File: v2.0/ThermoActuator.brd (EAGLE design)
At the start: 99.1 x 80 mm, 72 parts, among them IC1 ULN2003AD, IC2 PCF8574T, U1 CD74HCT4051_D_16

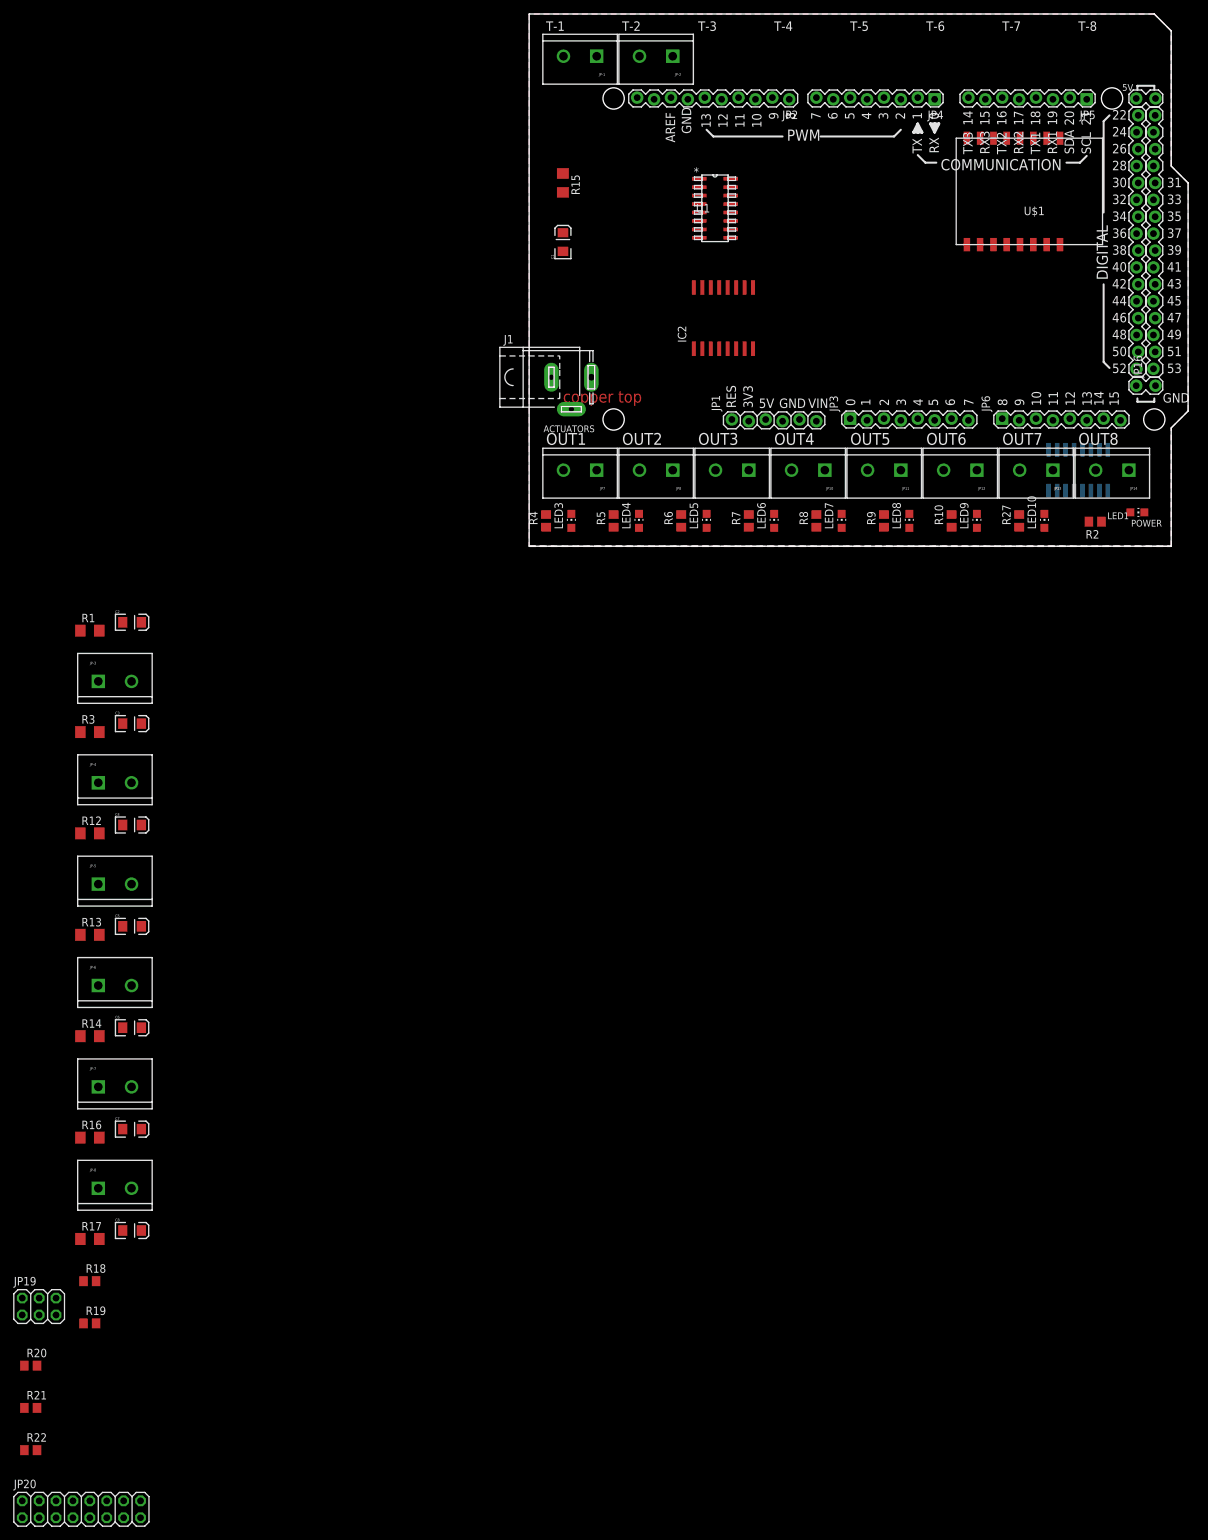
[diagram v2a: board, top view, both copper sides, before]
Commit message: PCB caped for lower profile
two capes are cut. All components are thrown on the PCB
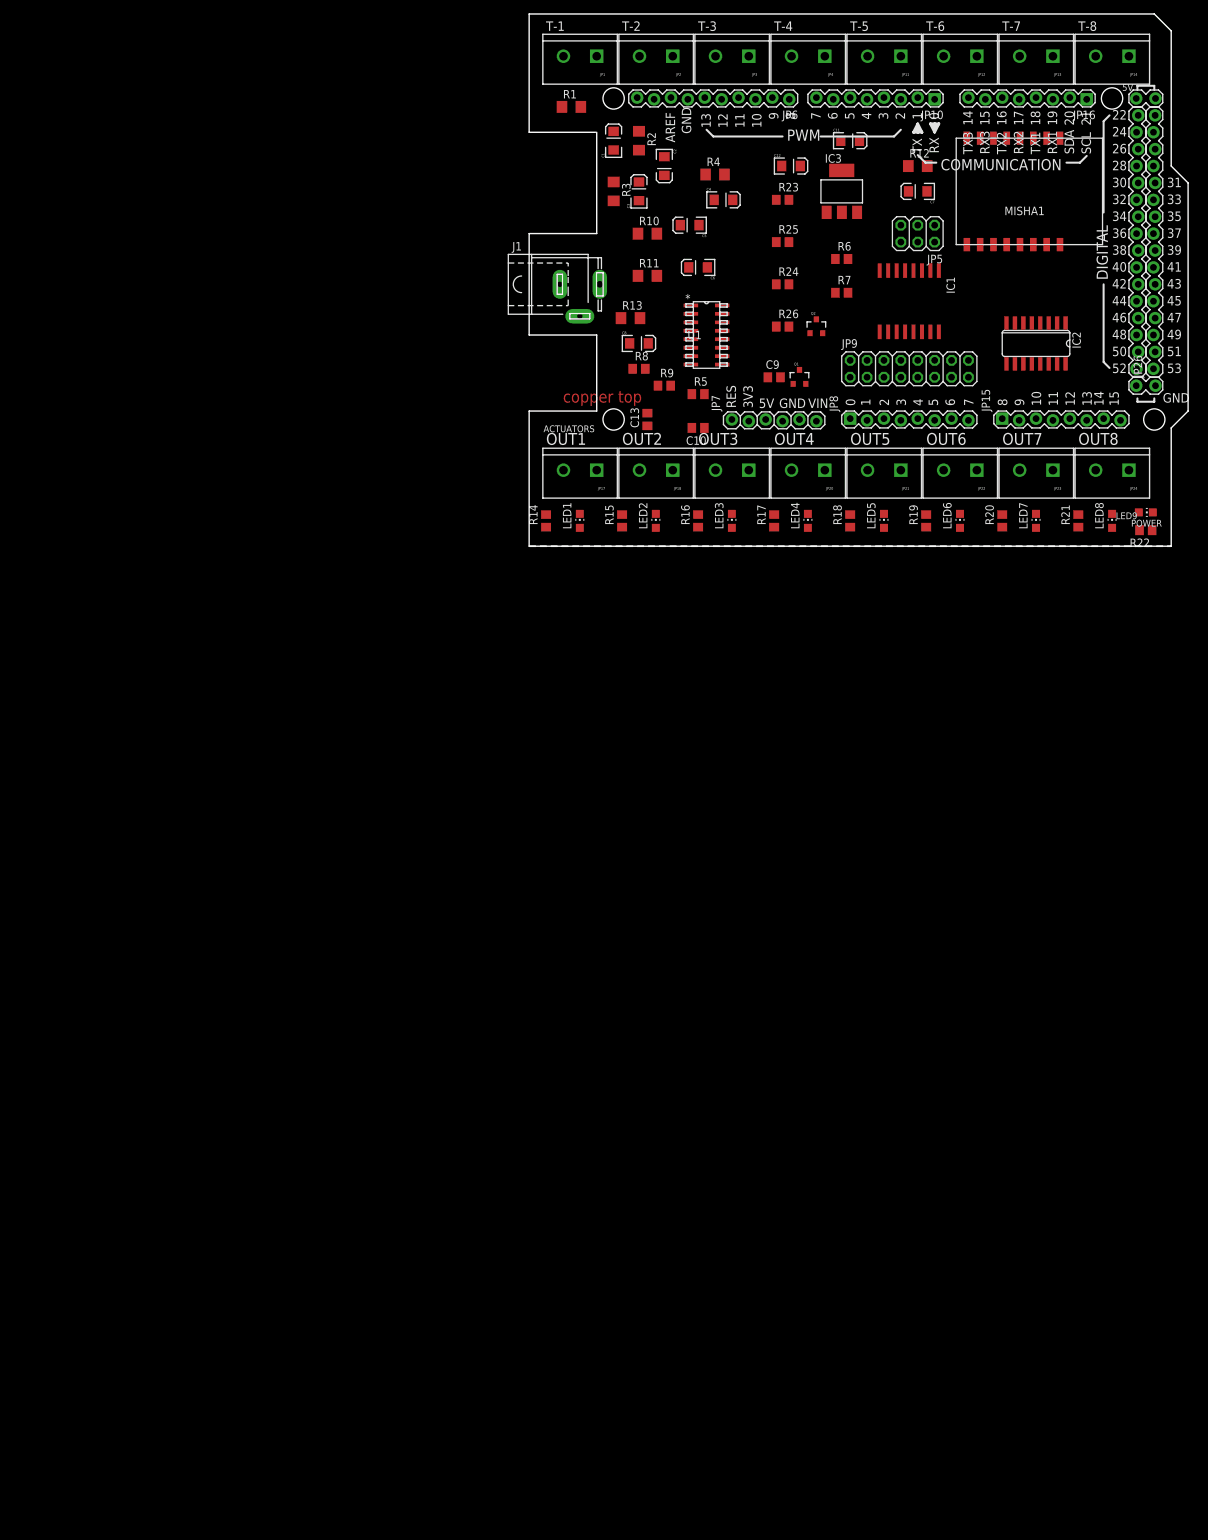
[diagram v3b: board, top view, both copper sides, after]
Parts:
- removed JP-1, JP-2, JP-3, JP-4, JP-5, JP-6, JP-7, JP-8: M025MM, SparkFun-Connectors:SCREWTERMINAL-5MM-2
- removed LED10: Blue, led:CHIP-LED0805
- removed R27: 330, rcl:R0805
- added C10, C13, C9: 100nF, rcl:C0805
- added C11, C12: 5uF, SparkFun-Capacitors:EIA3216
- added IC3: REG1117, burr-brown:SOT223
- added JP21, JP22, JP23, JP24: M025MM, SparkFun-Connectors:SCREWTERMINAL-5MM-2
- added JP25, JP28: (no value), SparkFun:1X02_LOCK
- added JP26, JP27: M16LOCK, SparkFun:1X16_LOCK
- added LED2: White, led:CHIP-LED0805
- added Q1, Q2: 200mA/50V, SparkFun-DiscreteSemi:SOT23-3
- added R11: 1K, rcl:R1206
- added R23, R24, R25, R26: 10K, rcl:R0805
- IC1: value ULN2003AD -> PCF8574T; device uln-udn:SO16 -> micro-philips:SO16W
- IC2: value PCF8574T -> ULN2003AD; device micro-philips:SO16W -> uln-udn:SO16
- JP1: value (none) -> M025MM; device SparkFun:1X06_LOCK -> SparkFun-Connectors:SCREWTERMINAL-5MM-2
- JP10, JP8: value M025MM -> (none); device SparkFun-Connectors:SCREWTERMINAL-5MM-2 -> SparkFun:1X08_LOCK
- JP15: device SparkFun:1X02_LOCK -> SparkFun:1X08_LOCK
- JP16: value M16LOCK -> (none); device SparkFun:1X16_LOCK -> SparkFun:1X08_LOCK
- JP17: value M16LOCK -> M025MM; device SparkFun:1X16_LOCK -> SparkFun-Connectors:SCREWTERMINAL-5MM-2
- JP18: value (none) -> M025MM; device SparkFun:1X02_LOCK -> SparkFun-Connectors:SCREWTERMINAL-5MM-2
- JP19: value (none) -> M025MM; device pinhead:2X03 -> SparkFun-Connectors:SCREWTERMINAL-5MM-2
- JP2: value M10LOCK -> M025MM; device SparkFun-Connectors:1X10_LOCK -> SparkFun-Connectors:SCREWTERMINAL-5MM-2
- JP20: value (none) -> M025MM; device pinhead:2X08 -> SparkFun-Connectors:SCREWTERMINAL-5MM-2
- JP3, JP4: value (none) -> M025MM; device SparkFun:1X08_LOCK -> SparkFun-Connectors:SCREWTERMINAL-5MM-2
- JP5: device SparkFun:1X08_LOCK -> pinhead:2X03
- JP6: value (none) -> M10LOCK; device SparkFun:1X08_LOCK -> SparkFun-Connectors:1X10_LOCK
- JP7: value M025MM -> (none); device SparkFun-Connectors:SCREWTERMINAL-5MM-2 -> SparkFun:1X06_LOCK
- JP9: value M025MM -> (none); device SparkFun-Connectors:SCREWTERMINAL-5MM-2 -> pinhead:2X08
- LED1: value Red -> White
- LED3, LED4, LED5, LED6, LED7, LED8: value Blue -> White
- R10, R2, R4: value 330 -> 1K; device rcl:R0805 -> rcl:R1206
- R14, R15, R16, R17: value 1K -> 3K3; device rcl:R1206 -> rcl:R0805
- R18, R19: value 330 -> 3K3
- R20, R21, R22: value 1K -> 3K3
- R5, R6, R7: value 330 -> 1K
- R8, R9: value 330 -> 4K7
- moved R22 217.3 mm to (92.7, 2.41), turned to 180 degrees
- moved R21 206.4 mm to (82.5, 3.81), turned to 90 degrees
- moved R20 193.5 mm to (71.1, 3.81), turned to 90 degrees
- moved JP20 192.1 mm to (44.5, 11.4), turned to 180 degrees
- moved C7 183.9 mm to (58.4, 53.3), turned to 180 degrees
- moved R19 174.3 mm to (59.7, 3.81), turned to 90 degrees
- moved JP19 164.9 mm to (33.0, 11.4), turned to 180 degrees
- moved R18 161.6 mm to (48.3, 3.81), turned to 90 degrees
- moved R12 159.9 mm to (58.4, 57.1)
- moved C8 153.6 mm to (16.5, 30.5)
- moved R17 149.1 mm to (36.8, 3.81), turned to 90 degrees
- moved C6 142.5 mm to (25.4, 41.9), turned to 180 degrees
- moved C5 134.7 mm to (24.1, 48.3), turned to 180 degrees
- moved R16 130.2 mm to (25.4, 3.81), turned to 90 degrees
- moved C4 129.4 mm to (29.2, 52.1)
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- renumbered U$1 to MISHA1
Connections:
- removed net D16: JP5.6
- removed net D17: JP5.5
- removed net D18: JP5.4
- removed net D19: JP5.3
- removed net GND: C1.C, C2.C, C3.C, C4.C, C5.C, C6.C, C7.C, C8.C, IC1.8, IC2.8, JP-1.1, JP-2.1, JP-3.1, JP-4.1, JP-5.1, JP-6.1, JP-7.1, JP-8.1, JP1.4, JP1.5, JP14.1, JP18.1, JP18.2, JP19.1, JP19.3, JP19.5, JP2.7, LED1.C, MISHA1.GND, U1.6, U1.7, U1.8
- removed net VCC: MISHA1.VCC
- new net 3V3: C12.A, C13.1, IC3.2, MISHA1.CH_PD, MISHA1.REST, MISHA1.VCC, Q1.1, Q2.1, R23.2, R24.2
- new net N$40: MISHA1.TXD, Q1.2, R23.1
- new net N$41: MISHA1.RXD, Q2.2, R24.1
- new net NNN: C1.C, C10.2, C11.C, C12.C, C13.2, C2.C, C3.C, C4.C, C5.C, C6.C, C7.C, C8.C, C9.2, IC1.8, IC2.8, IC3.1, J1.1, JP1.1, JP11.1, JP12.1, JP13.1, JP14.1, JP2.1, JP24.1, JP28.1, JP28.2, JP3.1, JP4.1, JP5.1, JP5.3, JP5.5, JP6.7, JP7.4, JP7.5, LED9.C, MISHA1.GND, U1.6, U1.7, U1.8
- new net RX1: JP16.3
- new net RX2: JP16.5, Q1.3, R25.1
- new net TX0: JP10.2
- new net TX2: JP16.6, Q2.3, R26.1
- net 3.3: now also JP7.2; no longer JP1.2
- net 5V: now also JP7.3; no longer JP1.3
- net AO0: now also IC2.16, JP17.2, LED1.C; no longer IC1.16, JP7.2, LED3.C
- net AO1: now also IC2.15, JP18.2, LED2.C; no longer IC1.15, JP8.2, LED4.C
- net AO2: now also IC2.14, JP19.2, LED3.C; no longer IC1.14, JP9.2, LED5.C
- net AO3: now also IC2.13, JP20.2, LED4.C; no longer IC1.13, JP10.2, LED6.C
- net AO4: now also IC2.12, JP21.2, LED5.C; no longer IC1.12, JP11.2, LED7.C
- net AO5: now also IC2.11, JP22.2, LED6.C; no longer IC1.11, JP12.2, LED8.C
- net AO6: now also IC2.10, JP23.2, LED7.C; no longer IC1.10, JP13.2, LED9.C
- net AO7: now also IC1.12, JP24.2, LED8.C; no longer JP14.2, LED10.C
- net AREF: now also JP6.8; no longer JP2.8
- net AS0: now also R1.2; no longer R15.2
- net AS1: now also R2.2; no longer R1.2
- net AS3: now also R4.2; no longer R12.2
- net AS4: now also R10.2; no longer R13.2
- net AS5: now also R11.2; no longer R14.2
- net AS6: now also R12.2; no longer R16.2
- net AS7: now also R13.2; no longer R17.2
- net D10: now also JP6.3, U1.9; no longer JP2.3
- net D11: now also JP6.4; no longer JP2.4
- net D12: now also JP6.5; no longer JP2.5
- net D13: now also JP6.6; no longer JP2.6
- net D14: now also JP16.8; no longer JP5.8
- net D15: now also JP16.7; no longer JP5.7
- net D2: now also JP10.3; no longer JP4.3
- net D22: now also JP27.1; no longer JP17.1
- net D23: now also JP26.16; no longer JP16.16
- net D24: now also JP27.2; no longer JP17.2
- net D25: now also JP26.15; no longer JP16.15
- net D26: now also JP27.3; no longer JP17.3
- net D27: now also JP26.14; no longer JP16.14
- net D28: now also JP27.4; no longer JP17.4
- net D29: now also JP26.13; no longer JP16.13
- net D3: now also JP10.4; no longer JP4.4
- net D30: now also JP27.5; no longer JP17.5
- net D31: now also JP26.12; no longer JP16.12
- net D32: now also JP27.6; no longer JP17.6
- net D33: now also JP26.11; no longer JP16.11
- net D34: now also JP27.7; no longer JP17.7
- net D35: now also JP26.10; no longer JP16.10
- net D36: now also JP27.8; no longer JP17.8
- net D37: now also JP26.9; no longer JP16.9
- net D38: now also JP27.9; no longer JP17.9
- net D39: now also JP26.8; no longer JP16.8
- net D4: now also JP10.5; no longer JP4.5
- net D40: now also JP27.10; no longer JP17.10
- net D41: now also JP26.7; no longer JP16.7
- net D42: now also JP27.11; no longer JP17.11
- net D43: now also JP26.6; no longer JP16.6
- net D44: now also JP27.12; no longer JP17.12
- net D45: now also JP26.5; no longer JP16.5
- net D46: now also JP27.13; no longer JP17.13
- net D47: now also JP26.4; no longer JP16.4
- net D48: now also JP27.14; no longer JP17.14
- net D49: now also JP26.3; no longer JP16.3
- net D5: now also JP10.6; no longer JP4.6, U1.11
- net D50: now also JP27.15; no longer JP17.15
- net D51: now also JP26.2; no longer JP16.2
- net D52: now also JP27.16; no longer JP17.16
- net D53: now also JP26.1; no longer JP16.1
- net D6: now also JP10.7; no longer JP4.7, U1.10
- net D7: now also JP10.8; no longer JP4.8, U1.9
- net D8: now also JP6.1, U1.11; no longer JP2.1
- net D9: now also JP6.2, U1.10; no longer JP2.2
- net N$1: now also JP1.2, R1.1; no longer JP-1.2, R15.1
- net N$10: now also IC1.1, JP5.2, R5.1; no longer IC2.1, JP19.2, R20.1
- net N$11: now also JP3.2; no longer JP-3.2
- net N$12: now also JP4.2, R4.1; no longer JP-4.2, R12.1
- net N$126: now also LED9.A, R22.1; no longer LED1.A, R2.1
- net N$13: now also LED1.A, R14.1; no longer LED3.A, R4.1
- net N$14: now also LED2.A, R15.1; no longer LED4.A, R5.1
- net N$15: now also LED3.A, R16.1; no longer LED5.A, R6.1
- net N$16: now also LED4.A, R17.1; no longer LED6.A, R7.1
- net N$17: now also LED5.A, R18.1; no longer LED7.A, R8.1
- net N$18: now also LED6.A, R19.1; no longer LED8.A, R9.1
- net N$19: now also LED7.A, R20.1; no longer LED9.A, R10.1
- net N$2: now also JP2.2, R2.1; no longer JP-2.2, R1.1
- net N$20: now also JP11.2, R10.1; no longer JP-5.2, R13.1
- net N$21: now also JP12.2, R11.1; no longer JP-6.2, R14.1
- net N$22: now also JP13.2, R12.1; no longer JP-7.2, R16.1
- net N$23: now also JP14.2, R13.1; no longer JP-8.2, R17.1
- net N$24: now also IC1.2, JP5.4, R6.1; no longer IC2.2, JP19.4, R21.1
- net N$25: now also IC1.3, JP5.6, R7.1; no longer IC2.3, JP19.6, R22.1
- net N$26: now also JP8.1, JP9.1; no longer JP20.1, JP3.1
- net N$27: now also JP8.2, JP9.3; no longer JP20.3, JP3.2
- net N$28: now also JP8.3, JP9.5; no longer JP20.5, JP3.3
- net N$29: now also JP8.4, JP9.7; no longer JP20.7, JP3.4
- net N$3: now also IC1.4, IC2.1; no longer IC1.1, IC2.4
- net N$30: now also JP8.5, JP9.9; no longer JP20.9, JP3.5
- net N$31: now also JP8.6, JP9.11; no longer JP20.11, JP3.6
- net N$32: now also LED8.A, R21.1; no longer LED10.A, R27.1
- net N$36: now also JP9.10, JP9.12, JP9.14, JP9.16, JP9.2, JP9.4, JP9.6, JP9.8; no longer JP20.10, JP20.12, JP20.14, JP20.16, JP20.2, JP20.4, JP20.6, JP20.8
- net N$37: now also JP8.7, JP9.13; no longer JP20.13, JP3.7
- net N$38: now also JP8.8, JP9.15; no longer JP20.15, JP3.8
- net N$4: now also IC1.5, IC2.2; no longer IC1.2, IC2.5
- net N$5: now also IC1.6, IC2.3; no longer IC1.3, IC2.6
- net N$6: now also IC1.7, IC2.4; no longer IC1.4, IC2.7
- net N$7: now also IC1.9, IC2.5; no longer IC1.5, IC2.9
- net N$8: now also IC1.10, IC2.6; no longer IC1.6, IC2.10
- net N$9: now also IC1.11, IC2.7; no longer IC1.7, IC2.11
- net RES: now also JP7.1; no longer JP1.1
- net RX0: now also JP10.1; no longer JP4.1
- net SCL: now also IC1.14, JP16.1, R9.1; no longer IC2.14, JP5.1, R19.1
- net SDA: now also IC1.15, JP16.2, R8.1; no longer IC2.15, JP5.2, R18.1
- net TX1: now also JP16.4; no longer JP4.2
- net VDD: now also C10.1, C11.A, C9.1, IC1.16, IC2.9, IC3.3, J1.3, JP17.1, JP18.1, JP19.1, JP20.1, JP21.1, JP22.1, JP23.1, JP25.1, JP25.2, R14.2, R15.2, R16.2, R17.2, R25.2, R26.2; no longer IC1.9, IC2.16, JP10.1, JP11.1, JP12.1, JP13.1, JP15.1, JP15.2, JP7.1, JP8.1, JP9.1, R10.2, R2.2, R27.2, R4.2
- net VIN: now also JP7.6; no longer JP1.6
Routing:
- removed copper zone on layer 1, net GND
- removed copper zone on layer 16, net GND
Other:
- outline, holes or cut-outs redrawn

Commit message: to the fab
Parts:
- removed JP17, JP18, JP19, JP20, JP21, JP22: M025MM, SparkFun-Connectors:SCREWTERMINAL-5MM-2
- removed LED1, LED2, LED3, LED4, LED5, LED6, LED7, LED8: White, led:CHIP-LED0805
- added 1, 2, 3, 4, 5, 6, 7, 8: (no value), led:CHIP-LED0805
- added C14: 100nF, rcl:C0805
- added D1: 1N4001, diode:D-10
- added R27: 10K, resistor:R0805
- added X1: (no value), con-phoenix-500:MSTBV8
- moved R14 86.4 mm to (88.9, 5.08), flipped to the bottom, turned to 270 degrees
- moved JP1 80.0 mm to (90.2, 73.7)
- moved JP14 80.0 mm to (10.2, 73.7)
- moved MISHA1 75.7 mm to (14.0, 10.2)
- moved R15 69.9 mm to (83.8, 5.08), flipped to the bottom, turned to 270 degrees
- moved LED9 67.3 mm to (25.4, 3.81), turned to 180 degrees
- moved R22 61.0 mm to (31.8, 3.68), flipped to the bottom
- moved R5 57.4 mm to (80.0, 40.6)
- moved JP13 57.1 mm to (21.6, 73.7)
- moved JP2 57.1 mm to (78.7, 73.7)
- moved R16 53.4 mm to (78.7, 5.08), flipped to the bottom, turned to 270 degrees
- moved R23 48.4 mm to (19.1, 7.62), flipped to the bottom, turned to 90 degrees
- moved R8 48.4 mm to (61.0, 45.7), turned to 180 degrees
- moved R1 47.7 mm to (48.3, 43.2), turned to 180 degrees
- moved R9 47.3 mm to (61.0, 48.3), turned to 180 degrees
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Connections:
- removed net NNN: C1.C, C10.2, C11.C, C12.C, C13.2, C2.C, C3.C, C4.C, C5.C, C6.C, C7.C, C8.C, C9.2, IC1.8, IC2.8, IC3.1, J1.1, JP1.1, JP11.1, JP12.1, JP13.1, JP14.1, JP2.1, JP24.1, JP28.1, JP28.2, JP3.1, JP4.1, JP5.1, JP5.3, JP5.5, JP6.7, JP7.4, JP7.5, LED9.C, MISHA1.GND, U1.6, U1.7, U1.8
- new net GND: C1.C, C10.2, C11.C, C12.C, C13.2, C14.2, C2.C, C3.C, C4.C, C5.C, C6.C, C7.C, C8.C, C9.2, IC1.8, IC2.8, IC3.1, J1.1, JP1.1, JP11.1, JP12.1, JP13.1, JP14.1, JP2.1, JP24.1, JP24.2, JP28.1, JP28.2, JP3.1, JP4.1, JP5.1, JP5.3, JP5.5, JP6.7, JP7.4, JP7.5, LED9.C, MISHA1.GND, U1.6, U1.7, U1.8
- new net N$42: D1.A, J1.3
- net AO0: now also 1.C, X1.1; no longer JP17.2, LED1.C
- net AO1: now also 2.C, X1.2; no longer JP18.2, LED2.C
- net AO2: now also 3.C, X1.3; no longer JP19.2, LED3.C
- net AO3: now also 4.C, X1.4; no longer JP20.2, LED4.C
- net AO4: now also 5.C, X1.5; no longer JP21.2, LED5.C
- net AO5: now also 6.C, X1.6; no longer JP22.2, LED6.C
- net AO6: now also 7.C, X1.7; no longer JP23.2, LED7.C
- net AO7: now also 8.C, X1.8; no longer JP24.2, LED8.C
- net N$13: now also 1.A; no longer LED1.A
- net N$14: now also 2.A; no longer LED2.A
- net N$15: now also 3.A; no longer LED3.A
- net N$16: now also 4.A; no longer LED4.A
- net N$17: now also 5.A; no longer LED5.A
- net N$18: now also 6.A; no longer LED6.A
- net N$19: now also 7.A; no longer LED7.A
- net N$32: now also 8.A; no longer LED8.A
- net N$36: now also R27.1
- net VDD: now also C14.1, D1.C, JP23.2, R27.2; no longer J1.3, JP17.1, JP18.1, JP19.1, JP20.1, JP21.1, JP22.1
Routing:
- net VDD: track 0.00 -> 451.9 mm, vias 0 -> 2
- net N$12: track 0.00 -> 79.2 mm, vias 0 -> 1
- net RX2: track 0.00 -> 79.1 mm, vias 0 -> 2
- net TX2: track 0.00 -> 79.1 mm, vias 0 -> 2
- net 3V3: track 0.00 -> 72.5 mm, vias 0 -> 1
- net N$21: track 0.00 -> 71.4 mm
- net AO7: track 0.00 -> 57.8 mm, vias 0 -> 1
- net N$1: track 0.00 -> 53.1 mm
- net N$36: track 0.00 -> 52.1 mm, vias 0 -> 1
- net AO1: track 0.00 -> 41.4 mm
- net AO0: track 0.00 -> 38.7 mm, vias 0 -> 1
- net SCL: track 0.00 -> 37.2 mm, vias 0 -> 1
- net N$25: track 0.00 -> 35.9 mm
- net N$2: track 0.00 -> 35.3 mm
- net SDA: track 0.00 -> 35.3 mm, vias 0 -> 1
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- added copper zone on layer 1, net GND
- added copper zone on layer 16, net GND
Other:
- board text added: "2-pin GND"
- board text added: "2-pin VDD"
- board text removed: "ACTUATORS"
- board text removed: "COMMUNICATION"
- board text removed: "OUT1"
- board text removed: "OUT2"
- board text removed: "OUT3"
- board text removed: "OUT4"
- board text removed: "OUT5"
- board text removed: "OUT6"
- board text removed: "OUT7"
- board text removed: "OUT8"
- board text removed: "copper top"
